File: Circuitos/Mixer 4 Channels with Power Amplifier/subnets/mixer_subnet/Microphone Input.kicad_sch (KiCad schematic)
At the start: 10 parts, among them SW1 SW_Push_DPDT, U4 ${SIM.PARAMS}

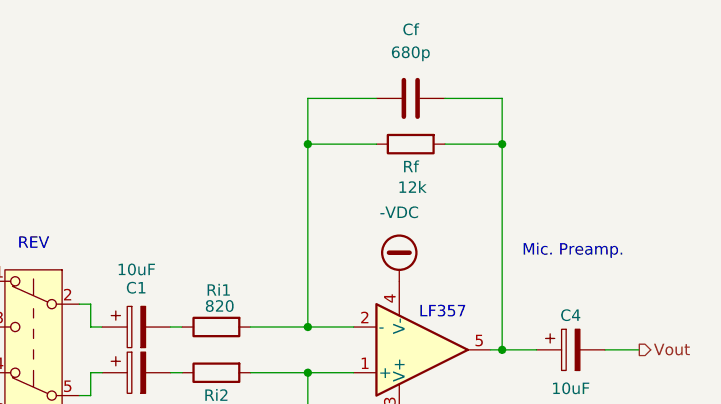
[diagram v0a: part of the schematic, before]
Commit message: Correcciones y modificaciones en fuente, amp auriculares y simul completa
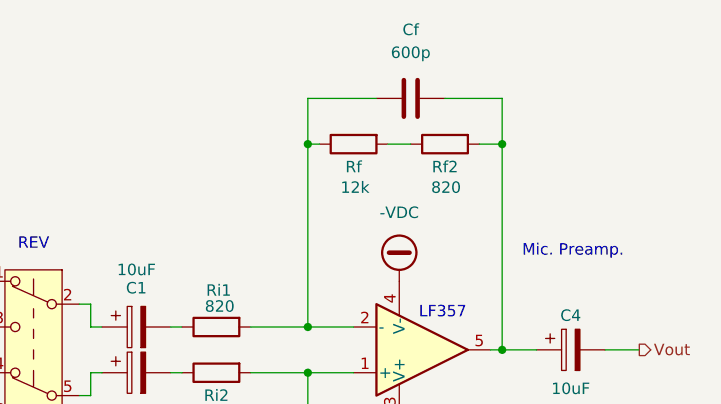
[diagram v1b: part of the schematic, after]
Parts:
- added Rf2: 820, symbol Device:R
- Cf: value 680p -> 600p
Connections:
- net at C4.1, Cf.2, U4.5: now also Rf2.2; no longer Rf.2
- new net: Rf.2, Rf2.1
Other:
- moved on the sheet: Rf
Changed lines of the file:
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@@
 	(wire
 		(pts
-			(xy 165.1 64.77) (xy 157.48 64.77)
+			(xy 158.75 64.77) (xy 157.48 64.77)
 		)
 		(stroke
@@
 	(wire
 		(pts
+			(xy 176.53 64.77) (xy 179.07 64.77)
+		)
+		(stroke
+			(width 0)
+			(type default)
+		)
+	)
+	(wire
+		(pts
 			(xy 118.11 85.09) (xy 118.11 90.17)
 		)
@@
 	(wire
 		(pts
-			(xy 172.72 64.77) (xy 179.07 64.77)
+			(xy 166.37 64.77) (xy 168.91 64.77)
 		)
 		(stroke
@@
 			)
 		)
-		(property "Value" "680p"
+		(property "Value" "600p"
 			(at 168.91 54.61 90)
 			(effects
@@
 				(path "/15464fd7-4efb-41cb-956d-8afc44b1c436"
 					(reference "Ri1")
+					(unit 1)
+				)
+			)
+		)
+	)
+	(symbol
+		(lib_id "Device:R")
+		(at 172.72 64.77 90)
+		(mirror x)
+		(unit 1)
+		(exclude_from_sim no)
+		(in_bom yes)
+		(on_board yes)
+		(dnp no)
+		(property "Reference" "Rf2"
+			(at 172.72 67.31 90)
+			(effects
+				(font
+					(size 1.27 1.27)
+				)
+			)
+		)
+		(property "Value" "820"
+			(at 174.498 69.596 90)
+			(effects
+				(font
+					(size 1.27 1.27)
+				)
+				(justify left)
+			)
+		)
+		(property "Footprint" ""
+			(at 172.72 62.992 90)
+			(effects
+				(font
+					(size 1.27 1.27)
+				)
+				(hide yes)
+			)
+		)
+		(property "Datasheet" "~"
+			(at 172.72 64.77 0)
+			(effects
+				(font
+					(size 1.27 1.27)
+				)
+				(hide yes)
+			)
+		)
+		(property "Description" "Resistor"
+			(at 172.72 64.77 0)
+			(effects
+				(font
+					(size 1.27 1.27)
+				)
+				(hide yes)
+			)
+		)
+		(pin "1"
+		)
+		(pin "2"
+		)
+		(instances
+			(project "Mixer 4 Channels with Power Amplifier"
+				(path "/0e2446e7-fd41-47c0-87b8-110c51786f7b/7f4f2712-287c-4d36-933e-3ea06b7ca144/33f6bd3d-c26f-4cae-b216-d9ee7b4e037e"
+					(reference "Rf2")
 					(unit 1)
 				)
@@
 	(symbol
 		(lib_id "Device:R")
-		(at 168.91 64.77 90)
+		(at 162.56 64.77 90)
 		(mirror x)
 		(unit 1)
@@
 		(dnp no)
 		(property "Reference" "Rf"
-			(at 168.91 67.31 90)
+			(at 162.56 67.31 90)
 			(effects
 				(font
@@
 		)
 		(property "Value" "12k"
-			(at 170.688 69.596 90)
+			(at 164.338 69.596 90)
 			(effects
 				(font
@@
 		)
 		(property "Footprint" ""
-			(at 168.91 62.992 90)
+			(at 162.56 62.992 90)
 			(effects
 				(font
@@
 		)
 		(property "Datasheet" "~"
-			(at 168.91 64.77 0)
+			(at 162.56 64.77 0)
 			(effects
 				(font
@@
 		)
 		(property "Description" "Resistor"
-			(at 168.91 64.77 0)
+			(at 162.56 64.77 0)
 			(effects
 				(font
@@
 				)
 				(path "/0e2446e7-fd41-47c0-87b8-110c51786f7b/7f4f2712-287c-4d36-933e-3ea06b7ca144/33f6bd3d-c26f-4cae-b216-d9ee7b4e037e"
-					(reference "Rf")
-					(unit 1)
-				)
+					(reference "Rf1")
+					(unit 1)
+				)
